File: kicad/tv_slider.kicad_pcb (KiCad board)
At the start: 2 copper layers, 1 part, among them U1 ESP32-C6-DEVKITC-1-N8

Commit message: top level schematic completed
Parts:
- added FID1: Fiducial, Fiducial:Fiducial_1mm_Mask2mm, F.Cu at (44.0, 45.0)
- added FID2: Fiducial, Fiducial:Fiducial_1mm_Mask2mm, F.Cu at (42.0, 123.5)
- added FID3: Fiducial, Fiducial:Fiducial_1mm_Mask2mm, F.Cu at (149.0, 126.0)
- added J1: Conn_01x02, TerminalBlock_RND:TerminalBlock_RND_205-00276_1x02_P5.00mm_Vertical, F.Cu at (144.7, 58.5)
- added J2: Conn_01x04, TerminalBlock_RND:TerminalBlock_RND_205-00278_1x04_P5.00mm_Vertical, F.Cu at (144.2, 117.0)
- added J3: Conn_01x06, TerminalBlock_RND:TerminalBlock_RND_205-00280_1x06_P5.00mm_Vertical, F.Cu at (144.5, 92.5)
- added J4: Conn_01x03, TerminalBlock_RND:TerminalBlock_RND_205-00277_1x03_P5.00mm_Vertical, F.Cu at (49.0, 53.5)
- added J5: Conn_01x03, TerminalBlock_RND:TerminalBlock_RND_205-00277_1x03_P5.00mm_Vertical, F.Cu at (48.8, 71.0)
- added J6: Conn_01x03, TerminalBlock_RND:TerminalBlock_RND_205-00277_1x03_P5.00mm_Vertical, F.Cu at (48.8, 88.5)
- added J7: Conn_01x03, TerminalBlock_RND:TerminalBlock_RND_205-00277_1x03_P5.00mm_Vertical, F.Cu at (49.0, 106.0)
- added U2: DRV8452DDWR, local_library:IC_DRV8452DDWR, F.Cu at (128.8, 75.8)
- moved U1 12.8 mm to (88.1, 93.3)

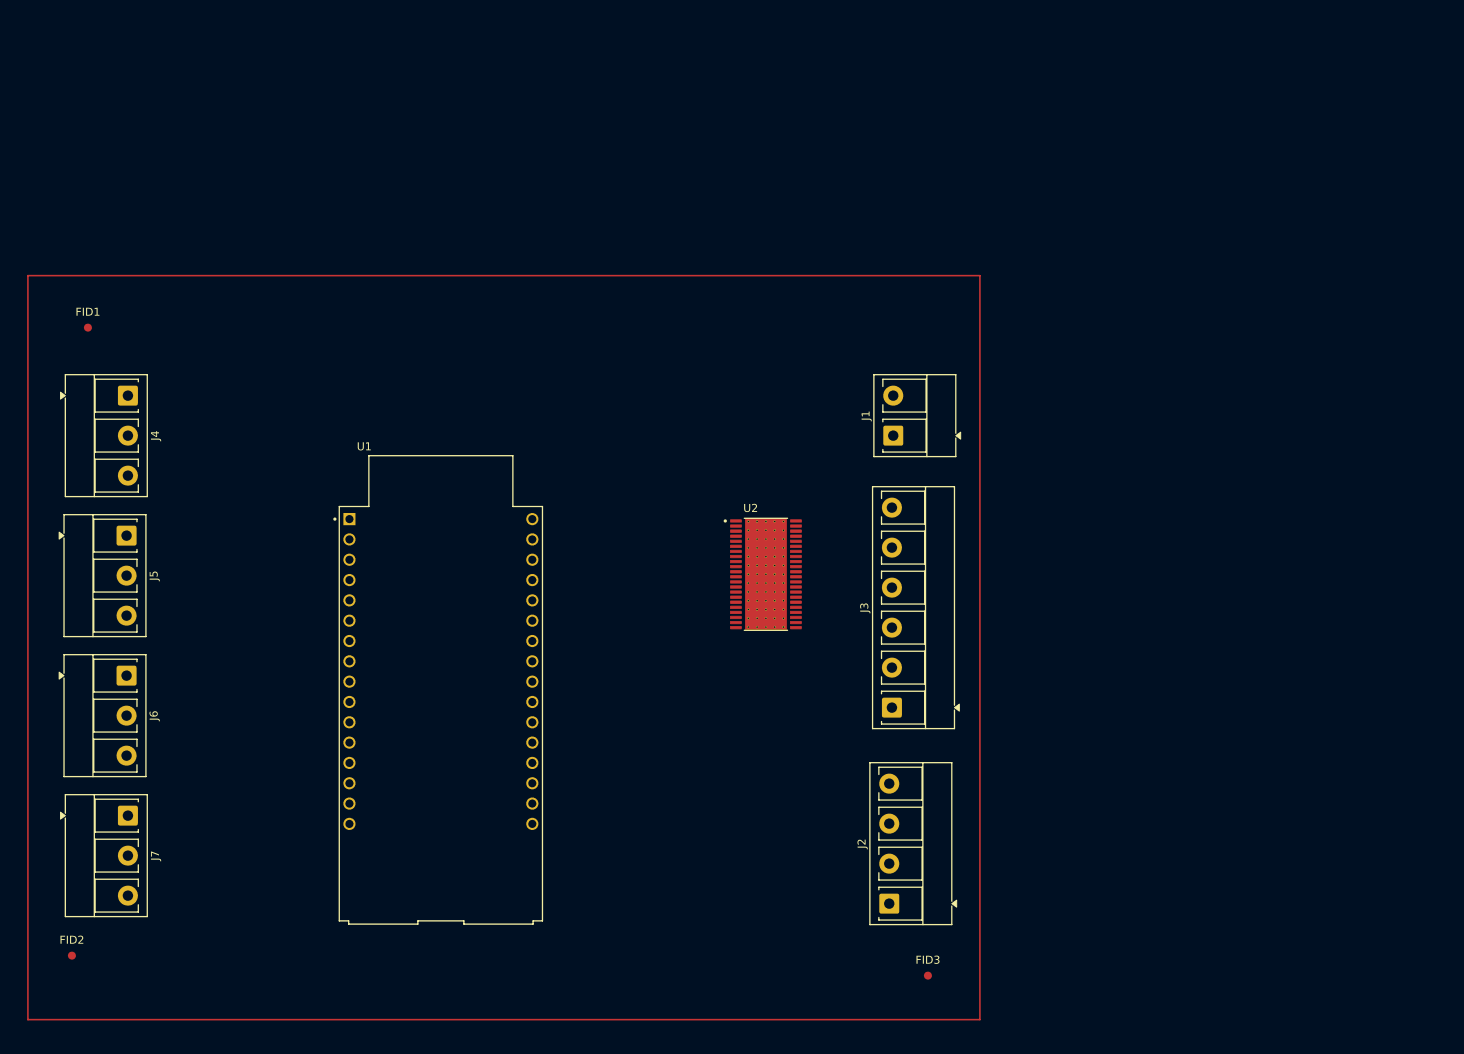
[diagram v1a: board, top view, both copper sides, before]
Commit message: Completed the schematic. All components have Digikey part numbers and footprints. The power supply sheet still requires some work.
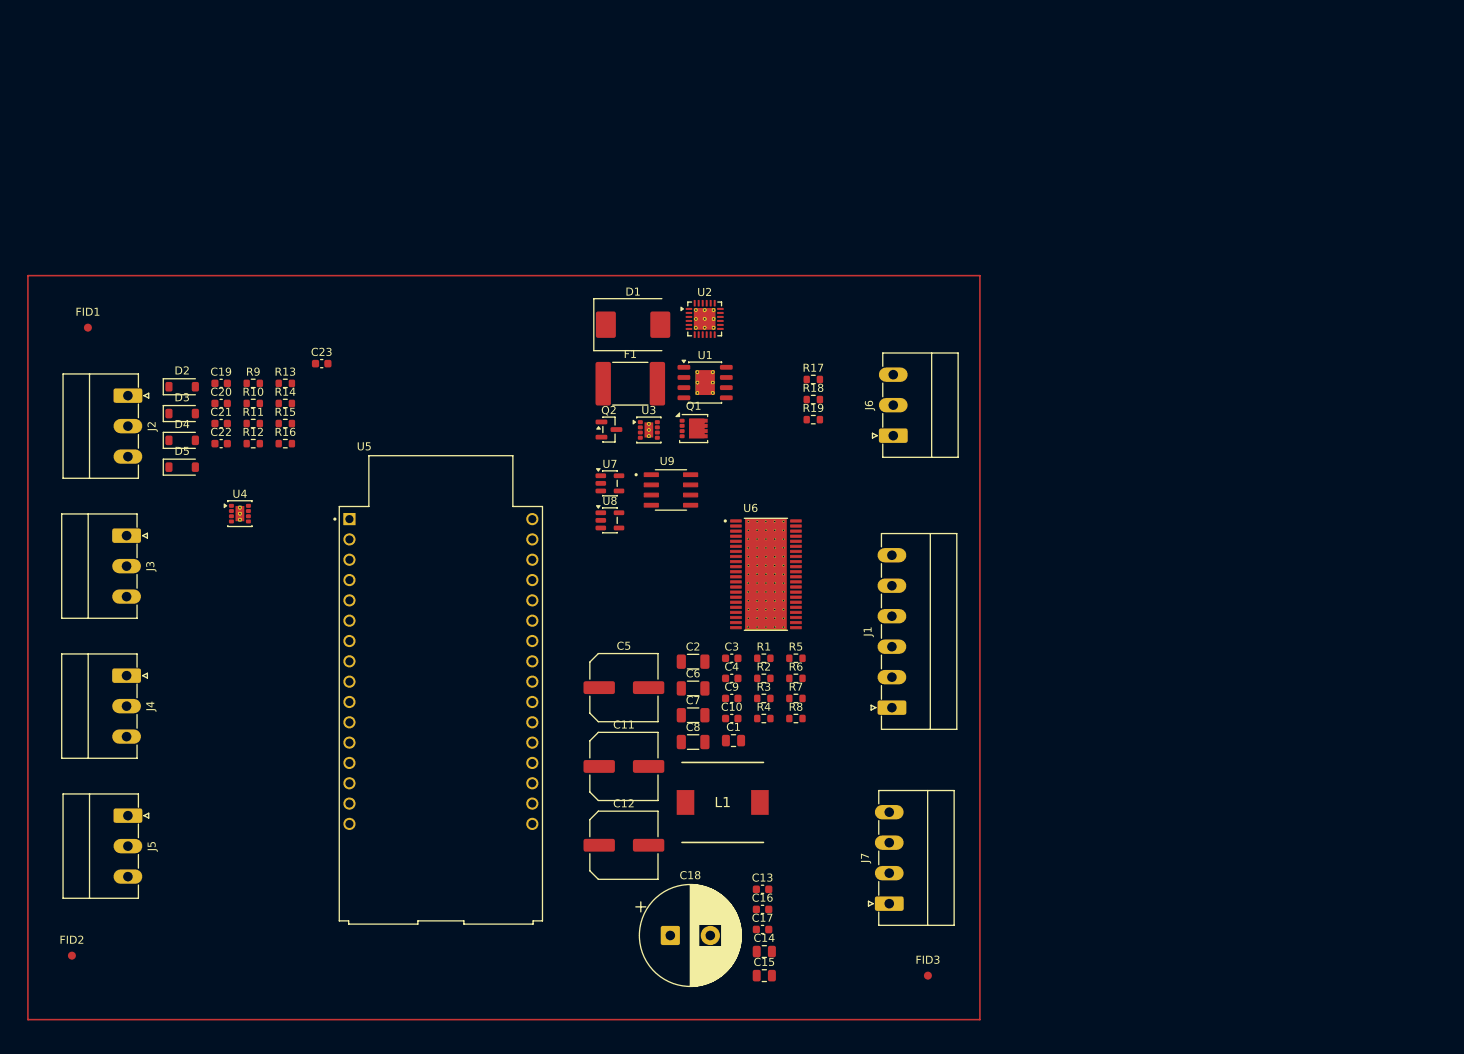
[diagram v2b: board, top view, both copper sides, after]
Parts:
- added C1: 1u, Capacitor_SMD:C_0805_2012Metric, F.Cu at (124.7, 96.6)
- added C10: 3.3n, Capacitor_SMD:C_0603_1608Metric, F.Cu at (124.5, 93.9)
- added C11: 22u, Capacitor_SMD:C_Elec_8x6.2, F.Cu at (111.0, 99.8)
- added C12: 22u, Capacitor_SMD:C_Elec_8x6.2, F.Cu at (111.0, 109.7)
- added C13: 100n, Capacitor_SMD:C_0603_1608Metric, F.Cu at (128.3, 115.2)
- added C14: 1u, Capacitor_SMD:C_0805_2012Metric, F.Cu at (128.6, 123.0)
- added C15: 1u, Capacitor_SMD:C_0805_2012Metric, F.Cu at (128.6, 126.0)
- added C16: 10n, Capacitor_SMD:C_0603_1608Metric, F.Cu at (128.3, 117.7)
- added C17: 10n, Capacitor_SMD:C_0603_1608Metric, F.Cu at (128.3, 120.2)
- added C18: 1000u, Capacitor_THT:CP_Radial_D12.5mm_P5.00mm, F.Cu at (116.8, 121.0)
- added C19: 22n, Capacitor_SMD:C_0603_1608Metric, F.Cu at (60.7, 52.0)
- added C2: 2.2u, Capacitor_SMD:C_1206_3216Metric, F.Cu at (119.7, 86.8)
- added C20: 22n, Capacitor_SMD:C_0603_1608Metric, F.Cu at (60.7, 54.5)
- added C21: 22n, Capacitor_SMD:C_0603_1608Metric, F.Cu at (60.7, 57.0)
- added C22: 22n, Capacitor_SMD:C_0603_1608Metric, F.Cu at (60.7, 59.5)
- added C23: 100n, Capacitor_SMD:C_0603_1608Metric, F.Cu at (73.2, 49.5)
- added C3: 2.2n, Capacitor_SMD:C_0603_1608Metric, F.Cu at (124.5, 86.3)
- added C4: 100n, Capacitor_SMD:C_0603_1608Metric, F.Cu at (124.5, 88.8)
- added C5: 47u, Capacitor_SMD:C_Elec_8x6.2, F.Cu at (111.0, 90.0)
- added C6: 2.2u, Capacitor_SMD:C_1206_3216Metric, F.Cu at (119.7, 90.1)
- added C7: 10u, Capacitor_SMD:C_1206_3216Metric, F.Cu at (119.7, 93.5)
- added C8: 10u, Capacitor_SMD:C_1206_3216Metric, F.Cu at (119.7, 96.8)
- added C9: 3.3n, Capacitor_SMD:C_0603_1608Metric, F.Cu at (124.5, 91.3)
- added D1: 1.5SMCxxCA, Diode_SMD:D_SMC, F.Cu at (112.1, 44.6)
- added D2: 3V6, Diode_SMD:D_SOD-123, F.Cu at (55.8, 52.4)
- added D3: 3V6, Diode_SMD:D_SOD-123, F.Cu at (55.8, 55.7)
- added D4: 3V6, Diode_SMD:D_SOD-123, F.Cu at (55.8, 59.1)
- added D5: 3V6, Diode_SMD:D_SOD-123, F.Cu at (55.8, 62.4)
- added F1: 1.1A, Fuse:Fuse_2920_7451Metric, F.Cu at (111.8, 52.0)
- added L1: 68u, local_library:INDPM102100X400N, F.Cu at (123.3, 104.3)
- added Q1: CSD19537Q3, Package_SON:VSON-8_3.3x3.3mm_P0.65mm_NexFET, F.Cu at (119.7, 57.6)
- added Q2: BSS138, Package_TO_SOT_SMD:SOT-23, F.Cu at (109.1, 57.7)
- added R1: 100k, Resistor_SMD:R_0603_1608Metric, F.Cu at (128.5, 86.3)
- added R10: 100, Resistor_SMD:R_0603_1608Metric, F.Cu at (64.7, 54.5)
- added R11: 10k, Resistor_SMD:R_0603_1608Metric, F.Cu at (64.7, 57.0)
- added R12: 10k, Resistor_SMD:R_0603_1608Metric, F.Cu at (64.7, 59.5)
- added R13: 100, Resistor_SMD:R_0603_1608Metric, F.Cu at (68.7, 52.0)
- added R14: 100, Resistor_SMD:R_0603_1608Metric, F.Cu at (68.7, 54.5)
- added R15: 10k, Resistor_SMD:R_0603_1608Metric, F.Cu at (68.7, 57.0)
- added R16: 10k, Resistor_SMD:R_0603_1608Metric, F.Cu at (68.7, 59.5)
- added R17: 120, Resistor_SMD:R_0603_1608Metric, F.Cu at (134.7, 51.5)
- added R18: 120, Resistor_SMD:R_0603_1608Metric, F.Cu at (134.7, 54.0)
- added R19: 100k, Resistor_SMD:R_0603_1608Metric, F.Cu at (134.7, 56.5)
- added R2: 448k, Resistor_SMD:R_0603_1608Metric, F.Cu at (128.5, 88.8)
- added R3: 49k9, Resistor_SMD:R_0603_1608Metric, F.Cu at (128.5, 91.3)
- added R4: 6.98k, Resistor_SMD:R_0603_1608Metric, F.Cu at (128.5, 93.9)
- added R5: 526k, Resistor_SMD:R_0603_1608Metric, F.Cu at (132.5, 86.3)
- added R6: 100k, Resistor_SMD:R_0603_1608Metric, F.Cu at (132.5, 88.8)
- added R7: 316k, Resistor_SMD:R_0603_1608Metric, F.Cu at (132.5, 91.3)
- added R8: 100k, Resistor_SMD:R_0603_1608Metric, F.Cu at (132.5, 93.9)
- added R9: 100, Resistor_SMD:R_0603_1608Metric, F.Cu at (64.7, 52.0)
- added U1: LM5164DDA, Package_SO:HSOP-8-1EP_3.9x4.9mm_P1.27mm_EP2.41x3.1mm_ThermalVias, F.Cu at (121.2, 51.9)
- added U2: TPS26632RGE, Package_DFN_QFN:Texas_RGE0024H_VQFN-24-1EP_4x4mm_P0.5mm_EP2.7x2.7mm_ThermalVias, F.Cu at (121.1, 43.9)
- added U3: TPS82130, Package_LGA:Texas_SIL0008D_MicroSiP-8-1EP_2.8x3mm_P0.65mm_EP1.1x1.9mm_ThermalVias, F.Cu at (114.1, 57.8)
- added U4: TPS82130, Package_LGA:Texas_SIL0008D_MicroSiP-8-1EP_2.8x3mm_P0.65mm_EP1.1x1.9mm_ThermalVias, F.Cu at (63.0, 68.2)
- added U7: ISL3280ExHZ, Package_TO_SOT_SMD:SOT-23-5, F.Cu at (109.2, 64.5)
- added U8: ISL3280ExHZ, Package_TO_SOT_SMD:SOT-23-5, F.Cu at (109.2, 69.1)
- added U9: LS7184N-S, local_library:SOIC127P600X175-8N, F.Cu at (116.9, 65.3)
- J1: renamed from J3; value Conn_01x06 -> MC 1,5/6-G-3.81; footprint TerminalBlock_RND:TerminalBlock_RND_205-00280_1x06_P5.00mm_Vertical -> Connector_Phoenix_MC:PhoenixContact_MC_1,5_6-G-3.81_1x06_P3.81mm_Horizontal
- J2: renamed from J4; value Conn_01x03 -> MC 1,5/3-G-3.81; footprint TerminalBlock_RND:TerminalBlock_RND_205-00277_1x03_P5.00mm_Vertical -> Connector_Phoenix_MC:PhoenixContact_MC_1,5_3-G-3.81_1x03_P3.81mm_Horizontal
- J3: renamed from J5; value Conn_01x03 -> MC 1,5/3-G-3.81; footprint TerminalBlock_RND:TerminalBlock_RND_205-00277_1x03_P5.00mm_Vertical -> Connector_Phoenix_MC:PhoenixContact_MC_1,5_3-G-3.81_1x03_P3.81mm_Horizontal
- J4: renamed from J6; value Conn_01x03 -> MC 1,5/3-G-3.81; footprint TerminalBlock_RND:TerminalBlock_RND_205-00277_1x03_P5.00mm_Vertical -> Connector_Phoenix_MC:PhoenixContact_MC_1,5_3-G-3.81_1x03_P3.81mm_Horizontal
- J5: renamed from J7; value Conn_01x03 -> MC 1,5/3-G-3.81; footprint TerminalBlock_RND:TerminalBlock_RND_205-00277_1x03_P5.00mm_Vertical -> Connector_Phoenix_MC:PhoenixContact_MC_1,5_3-G-3.81_1x03_P3.81mm_Horizontal
- J6: renamed from J1; value Conn_01x02 -> MC 1,5/3-G-3.81; footprint TerminalBlock_RND:TerminalBlock_RND_205-00276_1x02_P5.00mm_Vertical -> Connector_Phoenix_MC:PhoenixContact_MC_1,5_3-G-3.81_1x03_P3.81mm_Horizontal
- J7: renamed from J2; value Conn_01x04 -> MC 1,5/4-G-3.81; footprint TerminalBlock_RND:TerminalBlock_RND_205-00278_1x04_P5.00mm_Vertical -> Connector_Phoenix_MC:PhoenixContact_MC_1,5_4-G-3.81_1x04_P3.81mm_Horizontal
- renumbered U1 to U5, U2 to U6
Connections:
- J1 pad 1: /Shaft encoder/B+ -> GND
- J1 pad 2: /Shaft encoder/B- -> +5V
- J1 pad 3: /Shaft encoder/A+ -> /Shaft encoder/A-
- J1 pad 4: /Shaft encoder/A- -> /Shaft encoder/A+
- J1 pad 5: +3.3V -> /Shaft encoder/B-
- J1 pad 6: GND -> /Shaft encoder/B+
- J2 pad 2: /Location sensors/SENSOR_OUT_STOP -> GND
- J2 pad 3: GND -> /Location sensors/SENSOR_OUT_STOP
- J3 pad 2: /Location sensors/SENSOR_OUT_SLOW -> GND
- J3 pad 3: GND -> /Location sensors/SENSOR_OUT_SLOW
- J4 pad 2: /Location sensors/SENSOR_IN_SLOW -> GND
- J4 pad 3: GND -> /Location sensors/SENSOR_IN_SLOW
- J5 pad 2: /Location sensors/SENSOR_IN_STOP -> GND
- J5 pad 3: GND -> /Location sensors/SENSOR_IN_STOP
- J6 pad 1: /Power supply/Vin -> unconnected-(J6-Pin_1-Pad1)
- J7 pad 1: /Motor drive/A+ -> /Motor drive/B-
- J7 pad 2: /Motor drive/A- -> /Motor drive/B+
- J7 pad 3: /Motor drive/B+ -> /Motor drive/A-
- J7 pad 4: /Motor drive/B- -> /Motor drive/A+
- U5 pad J1_1: unconnected-(U1-ESP_3V3-PadJ1_1) -> +3V3
- U5 pad J1_10: unconnected-(U1-GPIO10-PadJ1_10) -> /Location sensors/OUT_STOP
- U5 pad J1_11: unconnected-(U1-GPIO11-PadJ1_11) -> /Location sensors/OUT_SLOW
- U5 pad J1_12: unconnected-(U1-GPIO2-PadJ1_12) -> /Location sensors/IN_SLOW
- U5 pad J1_13: unconnected-(U1-GPIO3-PadJ1_13) -> /Location sensors/IN_STOP
- U5 pad J1_15: unconnected-(U1-GND_J1_15-PadJ1_15) -> GND
- U5 pad J1_3: unconnected-(U1-GPIO4-PadJ1_3) -> /MCU/COUNT
- U5 pad J1_4: unconnected-(U1-GPIO5-PadJ1_4) -> /MCU/UP/~{DOWN}
- U5 pad J1_6: unconnected-(U1-GPIO7-PadJ1_6) -> /MCU/~{FAULT}
- U5 pad J3_1: unconnected-(U1-GND_J3_1-PadJ3_1) -> GND
- U5 pad J3_10: unconnected-(U1-GPIO18-PadJ3_10) -> /MCU/DIR
- U5 pad J3_11: unconnected-(U1-GPIO9-PadJ3_11) -> /MCU/STEP
- U5 pad J3_12: unconnected-(U1-GND_J3_12-PadJ3_12) -> GND
- U5 pad J3_13: unconnected-(U1-GPIO13-PadJ3_13) -> /MCU/~{SLEEP}
- U5 pad J3_15: unconnected-(U1-GND_J3_15-PadJ3_15) -> GND
- U5 pad J3_4: unconnected-(U1-GPIO15-PadJ3_4) -> /MCU/~{CS}
- U5 pad J3_5: unconnected-(U1-GPIO23-PadJ3_5) -> /MCU/SCLK
- U5 pad J3_6: unconnected-(U1-GPIO22-PadJ3_6) -> /MCU/MOSI
- U5 pad J3_7: unconnected-(U1-GPIO21-PadJ3_7) -> /MCU/MISO
- U5 pad J3_9: unconnected-(U1-GPIO19-PadJ3_9) -> /MCU/ENABLE
- U6 pad 1: unconnected-(U2-VCP-Pad1) -> Net-(U6-VCP)
- U6 pad 10: unconnected-(U2-PGNDA__1-Pad10) -> GND
- U6 pad 11: unconnected-(U2-VM__1-Pad11) -> Vdrive
- U6 pad 12: unconnected-(U2-VM__2-Pad12) -> Vdrive
- U6 pad 13: unconnected-(U2-PGNDB-Pad13) -> GND
- U6 pad 14: unconnected-(U2-BOUT2-Pad14) -> /Motor drive/B-
- U6 pad 15: unconnected-(U2-BOUT2__1-Pad15) -> /Motor drive/B-
- U6 pad 16: unconnected-(U2-BOUT2__2-Pad16) -> /Motor drive/B-
- U6 pad 17: unconnected-(U2-BOUT1-Pad17) -> /Motor drive/B+
- U6 pad 18: unconnected-(U2-BOUT1__1-Pad18) -> /Motor drive/B+
- U6 pad 19: unconnected-(U2-BOUT1__2-Pad19) -> /Motor drive/B+
- U6 pad 2: unconnected-(U2-VM-Pad2) -> Vdrive
- U6 pad 20: unconnected-(U2-PGNDB__1-Pad20) -> GND
- U6 pad 21: unconnected-(U2-VM__3-Pad21) -> Vdrive
- U6 pad 22: unconnected-(U2-GND-Pad22) -> GND
- U6 pad 23: unconnected-(U2-GND__1-Pad23) -> GND
- U6 pad 24: unconnected-(U2-DVDD-Pad24) -> Net-(U6-DVDD)
- U6 pad 25: unconnected-(U2-VCC-Pad25) -> +3V3
- U6 pad 26: unconnected-(U2-~{FAULT}-Pad26) -> /MCU/~{FAULT}
- U6 pad 28: unconnected-(U2-MODE-Pad28) -> +3V3
- U6 pad 3: unconnected-(U2-PGNDA-Pad3) -> GND
- U6 pad 34: unconnected-(U2-~{SCS}/M0-Pad34) -> /MCU/~{CS}
- U6 pad 36: unconnected-(U2-SDO/DECAY1-Pad36) -> /MCU/MISO
- U6 pad 37: unconnected-(U2-SDI/DECAY0-Pad37) -> /MCU/MOSI
- U6 pad 38: unconnected-(U2-SCLK/M1-Pad38) -> /MCU/SCLK
- U6 pad 39: unconnected-(U2-STEP-Pad39) -> /MCU/STEP
- U6 pad 4: unconnected-(U2-AOUT1-Pad4) -> /Motor drive/A+
- U6 pad 40: unconnected-(U2-DIR-Pad40) -> /MCU/DIR
- U6 pad 41: unconnected-(U2-ENABLE-Pad41) -> /MCU/ENABLE
- U6 pad 42: unconnected-(U2-~{SLEEP}-Pad42) -> /MCU/~{SLEEP}
- U6 pad 43: unconnected-(U2-CPL-Pad43) -> Net-(U6-CPL)
- U6 pad 44: unconnected-(U2-CPH-Pad44) -> Net-(U6-CPH)
- U6 pad 45: unconnected-(U2-EXP-Pad45) -> GND
- U6 pad 5: unconnected-(U2-AOUT1__1-Pad5) -> /Motor drive/A+
- U6 pad 6: unconnected-(U2-AOUT1__2-Pad6) -> /Motor drive/A+
- U6 pad 7: unconnected-(U2-AOUT2-Pad7) -> /Motor drive/A-
- U6 pad 8: unconnected-(U2-AOUT2__1-Pad8) -> /Motor drive/A-
- U6 pad 9: unconnected-(U2-AOUT2__2-Pad9) -> /Motor drive/A-

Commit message: Updated footprints and step models. Placed on PCB, but not yet positioned in final location.
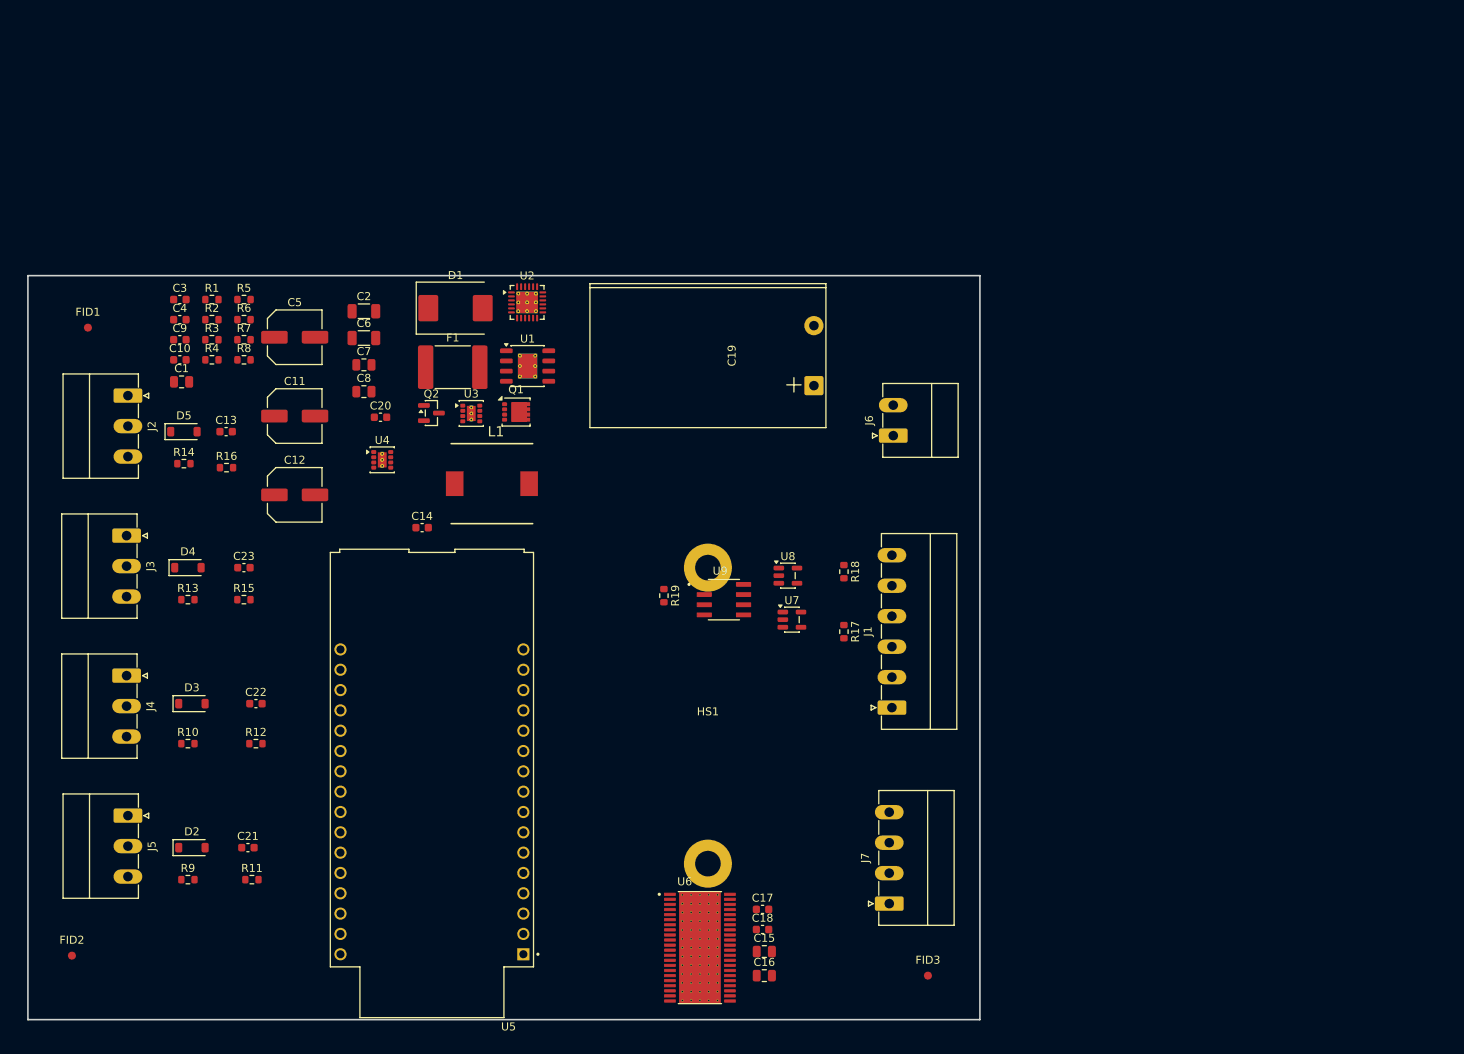
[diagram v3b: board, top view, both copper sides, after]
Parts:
- added HS1: Heatsink_Pad, local_library:ATS-TI1OP-519-C1-R3, F.Cu at (121.5, 93.5)
- C11, C12, C5: footprint Capacitor_SMD:C_Elec_8x6.2 -> Capacitor_SMD:C_Elec_6.3x5.8
- C19: renamed from C18; value 1000u -> 470u; footprint Capacitor_THT:CP_Radial_D12.5mm_P5.00mm -> local_library:CP_Radial_D18.0mm_P7.50mm_Horizontal
- C7, C8: footprint Capacitor_SMD:C_1206_3216Metric -> Capacitor_SMD:C_0805_2012Metric
- F1: footprint Fuse:Fuse_2920_7451Metric -> local_library:Fuse_2920_7451Metric
- J6: value MC 1,5/3-G-3.81 -> MC 1,5/2-G-3.81; footprint Connector_Phoenix_MC:PhoenixContact_MC_1,5_3-G-3.81_1x03_P3.81mm_Horizontal -> Connector_Phoenix_MC:PhoenixContact_MC_1,5_2-G-3.81_1x02_P3.81mm_Horizontal
- U3, U4: footprint Package_LGA:Texas_SIL0008D_MicroSiP-8-1EP_2.8x3mm_P0.65mm_EP1.1x1.9mm_ThermalVias -> local_library:Texas_SIL0008D_MicroSiP-8-1EP_2.8x3mm_P0.65mm_EP1.1x1.9mm_ThermalVias
- moved C1 82.3 mm to (55.7, 51.8)
- moved C10 82.3 mm to (55.5, 49.0)
- moved C3 82.3 mm to (55.5, 41.5)
- moved C4 82.3 mm to (55.5, 44.0)
- moved C9 82.3 mm to (55.5, 46.5)
- moved R1 82.3 mm to (59.5, 41.5)
- moved R2 82.3 mm to (59.5, 44.0)
- moved R3 82.3 mm to (59.5, 46.5)
- moved R4 82.3 mm to (59.5, 49.0)
- moved R5 82.3 mm to (63.5, 41.5)
- moved R6 82.3 mm to (63.5, 44.0)
- moved R7 82.3 mm to (63.5, 46.5)
- moved R8 82.3 mm to (63.5, 49.0)
- moved C19 71.0 mm to (134.8, 52.2), turned to 90 degrees
- moved R9 62.6 mm to (56.5, 114.0)
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- renumbered C23 to C13, C13 to C14, C14 to C15, C15 to C16, C16 to C17, C17 to C18, C19 to C20, C20 to C21, C21 to C22, C22 to C23
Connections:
- C5 pad 1: +12V -> Net-(C5-Pad1)
- F1 pad 1: +12V -> Net-(C5-Pad1)
- J6 pad 1: unconnected-(J6-Pin_1-Pad1) -> GND
- J6 pad 2: GND -> /Power supply/Vin
- L1 pad 2: +12V -> Net-(C5-Pad1)
- R2 pad 1: +12V -> Net-(C5-Pad1)
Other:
- board outline added: 119 x 93 mm
